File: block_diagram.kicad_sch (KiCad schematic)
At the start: 0 parts

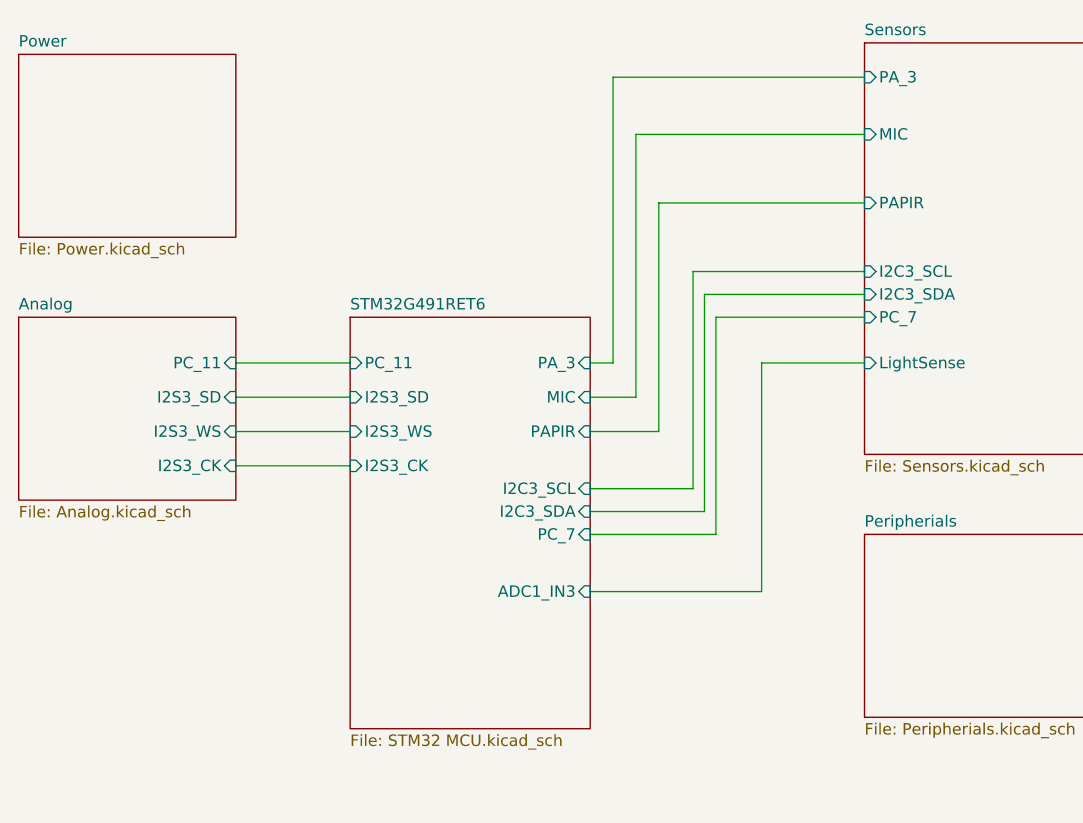
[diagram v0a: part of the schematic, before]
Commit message: fixing audio dac, moving audio to analog section
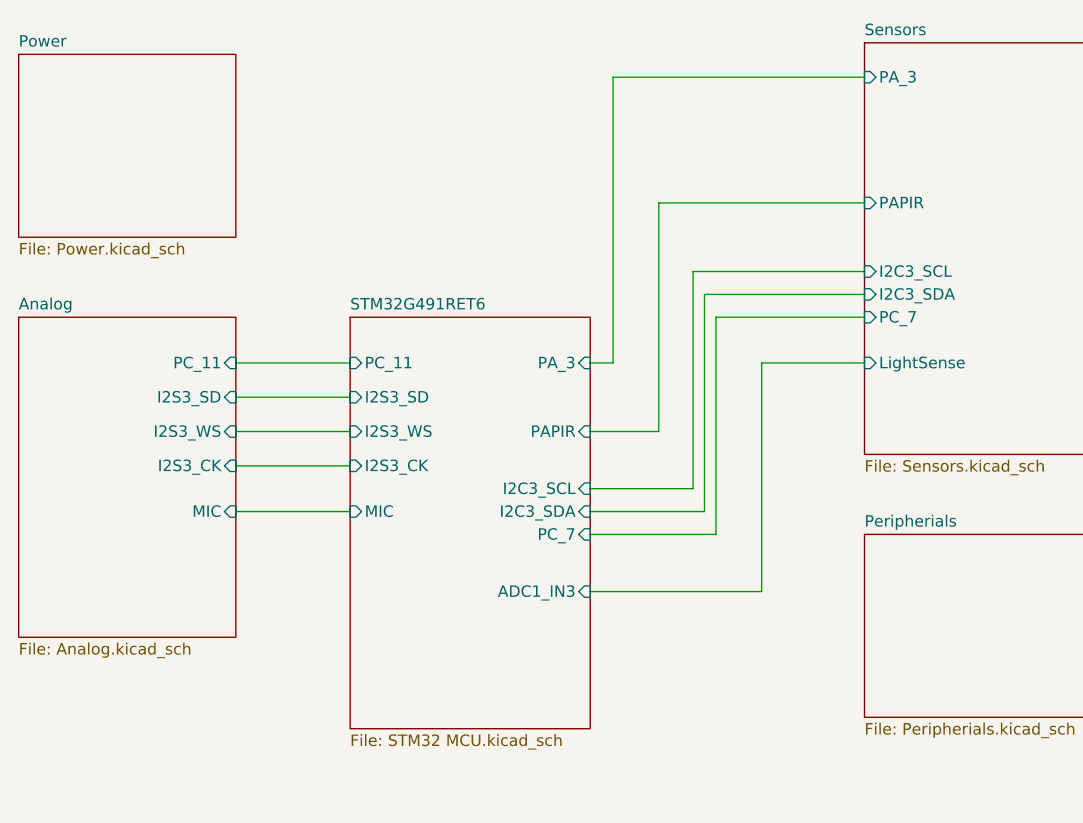
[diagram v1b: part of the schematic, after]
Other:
- sheet Analog ports: added MIC; removed none
- sheet Sensors ports: added none; removed MIC
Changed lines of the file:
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@@
 	(wire
 		(pts
-			(xy 146.05 87.63) (xy 140.97 87.63)
-		)
-		(stroke
-			(width 0)
-			(type default)
-		)
-	)
-	(wire
-		(pts
-			(xy 171.45 58.42) (xy 146.05 58.42)
+			(xy 101.6 100.33) (xy 114.3 100.33)
 		)
 		(stroke
@@
 		)
 	)
-	(wire
-		(pts
-			(xy 146.05 58.42) (xy 146.05 87.63)
-		)
-		(stroke
-			(width 0)
-			(type default)
-		)
-	)
 	(sheet
 		(at 114.3 78.74)
@@
 		)
 		(pin "MIC" input
-			(at 140.97 87.63 0)
-			(effects
-				(font
-					(size 1.27 1.27)
-				)
-				(justify right)
+			(at 114.3 100.33 180)
+			(effects
+				(font
+					(size 1.27 1.27)
+				)
+				(justify left)
 			)
 		)
@@
 			)
 		)
-		(pin "MIC" input
-			(at 171.45 58.42 180)
-			(effects
-				(font
-					(size 1.27 1.27)
-				)
-				(justify left)
-			)
-		)
 		(pin "I2C3_SCL" input
 			(at 171.45 73.66 180)
@@
 	(sheet
 		(at 77.47 78.74)
-		(size 24.13 20.32)
+		(size 24.13 35.56)
 		(exclude_from_sim no)
 		(in_bom yes)
@@
 		)
 		(property "Sheetfile" "Analog.kicad_sch"
-			(at 77.47 99.6446 0)
+			(at 77.47 114.8846 0)
 			(show_name no)
 			(do_not_autoplace no)
@@
 			(effects
 				(font
+					(size 1.27 1.27)
+				)
+				(justify right)
+			)
+		)
+		(pin "MIC" input
+			(at 101.6 100.33 0)
+			(effects
+				(font

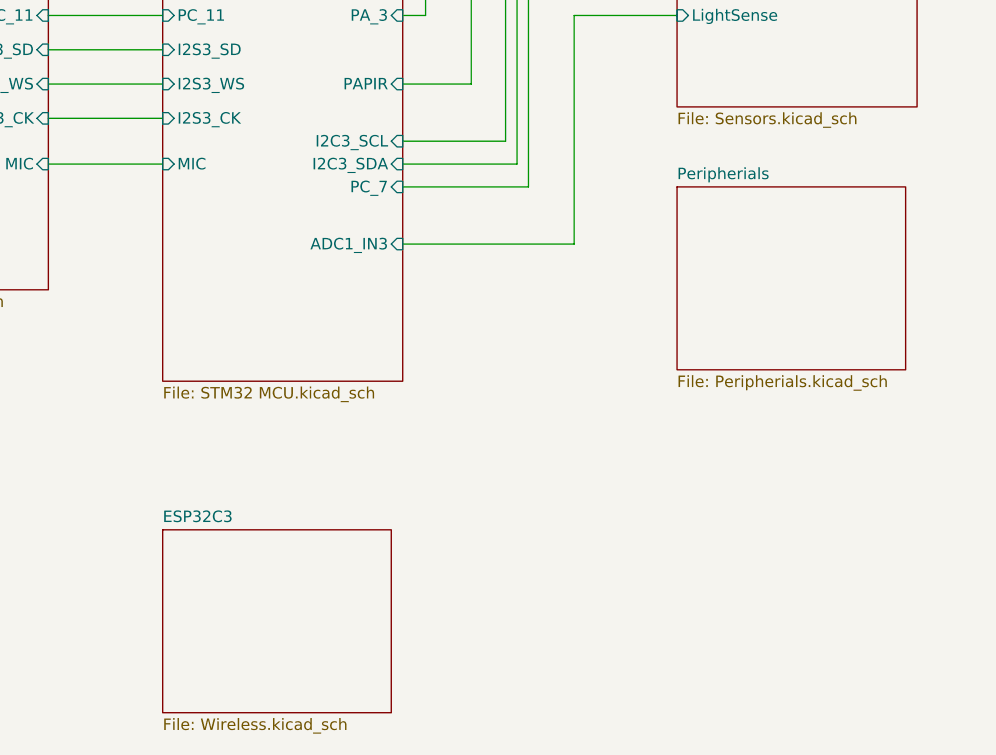
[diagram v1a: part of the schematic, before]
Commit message: added RTC
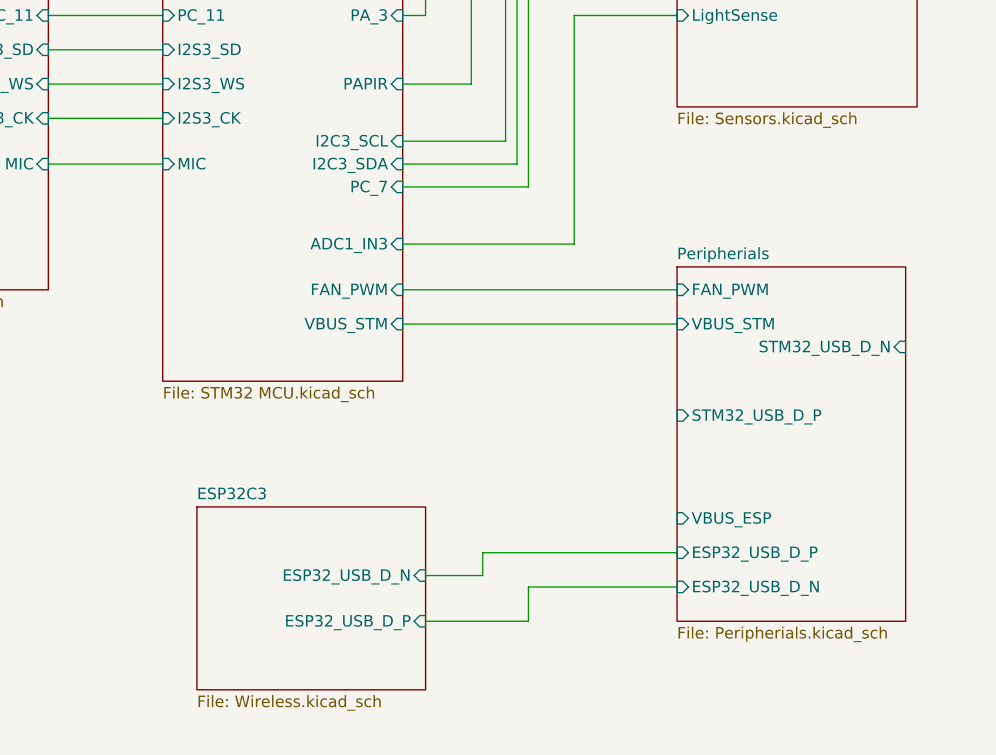
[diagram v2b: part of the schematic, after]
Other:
- sheet ESP32C3 ports: added ESP32_USB_D_N, ESP32_USB_D_P; removed none
- sheet Peripherials ports: added ESP32_USB_D_N, ESP32_USB_D_P, FAN_PWM, STM32_USB_D_N, STM32_USB_D_P, VBUS_ESP, VBUS_STM; removed none
- sheet STM32G491RET6 ports: added FAN_PWM, VBUS_STM; removed none
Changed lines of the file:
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@@
+	(wire
+		(pts
+			(xy 154.94 147.32) (xy 171.45 147.32)
+		)
+		(stroke
+			(width 0)
+			(type default)
+		)
+	)
 	(wire
 		(pts
@@
 	(wire
 		(pts
+			(xy 143.51 151.13) (xy 154.94 151.13)
+		)
+		(stroke
+			(width 0)
+			(type default)
+		)
+	)
+	(wire
+		(pts
+			(xy 140.97 118.11) (xy 171.45 118.11)
+		)
+		(stroke
+			(width 0)
+			(type default)
+		)
+	)
+	(wire
+		(pts
 			(xy 152.4 73.66) (xy 171.45 73.66)
 		)
@@
 	(wire
 		(pts
+			(xy 149.86 143.51) (xy 171.45 143.51)
+		)
+		(stroke
+			(width 0)
+			(type default)
+		)
+	)
+	(wire
+		(pts
 			(xy 101.6 91.44) (xy 114.3 91.44)
 		)
@@
 	(wire
 		(pts
+			(xy 149.86 146.05) (xy 149.86 143.51)
+		)
+		(stroke
+			(width 0)
+			(type default)
+		)
+	)
+	(wire
+		(pts
+			(xy 143.51 146.05) (xy 149.86 146.05)
+		)
+		(stroke
+			(width 0)
+			(type default)
+		)
+	)
+	(wire
+		(pts
 			(xy 140.97 91.44) (xy 148.59 91.44)
 		)
@@
 	(wire
 		(pts
+			(xy 140.97 114.3) (xy 171.45 114.3)
+		)
+		(stroke
+			(width 0)
+			(type default)
+		)
+	)
+	(wire
+		(pts
 			(xy 154.94 78.74) (xy 154.94 102.87)
 		)
@@
 		(pts
 			(xy 101.6 100.33) (xy 114.3 100.33)
+		)
+		(stroke
+			(width 0)
+			(type default)
+		)
+	)
+	(wire
+		(pts
+			(xy 154.94 151.13) (xy 154.94 147.32)
 		)
 		(stroke
@@
 			)
 		)
+		(pin "FAN_PWM" input
+			(at 140.97 114.3 0)
+			(effects
+				(font
+					(size 1.27 1.27)
+				)
+				(justify right)
+			)
+		)
+		(pin "VBUS_STM" input
+			(at 140.97 118.11 0)
+			(effects
+				(font
+					(size 1.27 1.27)
+				)
+				(justify right)
+			)
+		)
 		(instances
 			(project "SeniorDesign_PCB"
@@
 	)
 	(sheet
-		(at 114.3 140.97)
+		(at 118.11 138.43)
 		(size 25.4 20.32)
 		(exclude_from_sim no)
@@
 		)
 		(property "Sheetname" "ESP32C3"
-			(at 114.3 140.2584 0)
+			(at 118.11 137.7184 0)
 			(show_name no)
 			(do_not_autoplace no)
@@
 		)
 		(property "Sheetfile" "Wireless.kicad_sch"
-			(at 114.3 161.8746 0)
+			(at 118.11 159.3346 0)
 			(show_name no)
 			(do_not_autoplace no)
@@
 				)
 				(justify left top)
+			)
+		)
+		(pin "ESP32_USB_D_N" input
+			(at 143.51 146.05 0)
+			(effects
+				(font
+					(size 1.27 1.27)
+				)
+				(justify right)
+			)
+		)
+		(pin "ESP32_USB_D_P" input
+			(at 143.51 151.13 0)
+			(effects
+				(font
+					(size 1.27 1.27)
+				)
+				(justify right)
 			)
 		)
@@
 	)
 	(sheet
-		(at 171.45 102.87)
-		(size 25.4 20.32)
+		(at 171.45 111.76)
+		(size 25.4 39.37)
 		(exclude_from_sim no)
 		(in_bom yes)
@@
 		)
 		(property "Sheetname" "Peripherials"
-			(at 171.45 102.1584 0)
+			(at 171.45 111.0484 0)
 			(show_name no)
 			(do_not_autoplace no)
@@
 		)
 		(property "Sheetfile" "Peripherials.kicad_sch"
-			(at 171.45 123.7746 0)
+			(at 171.45 151.7146 0)
 			(show_name no)
 			(do_not_autoplace no)
@@
 			)
 		)
+		(pin "ESP32_USB_D_N" input
+			(at 171.45 147.32 180)
+			(effects
+				(font
+					(size 1.27 1.27)
+				)
+				(justify left)
+			)
+		)
+		(pin "ESP32_USB_D_P" input
+			(at 171.45 143.51 180)
+			(effects
+				(font
+					(size 1.27 1.27)
+				)
+				(justify left)
+			)
+		)
+		(pin "FAN_PWM" input
+			(at 171.45 114.3 180)
+			(effects
+				(font
+					(size 1.27 1.27)
+				)
+				(justify left)
+			)
+		)
+		(pin "STM32_USB_D_N" input
+			(at 196.85 120.65 0)
+			(effects
+				(font
+					(size 1.27 1.27)
+				)
+				(justify right)
+			)
+		)
+		(pin "STM32_USB_D_P" input
+			(at 171.45 128.27 180)
+			(effects
+				(font
+					(size 1.27 1.27)
+				)
+				(justify left)
+			)
+		)
+		(pin "VBUS_ESP" input
+			(at 171.45 139.7 180)
+			(effects
+				(font
+					(size 1.27 1.27)
+				)
+				(justify left)
+			)
+		)
+		(pin "VBUS_STM" input
+			(at 171.45 118.11 180)
+			(effects
+				(font
+					(size 1.27 1.27)
+				)
+				(justify left)
+			)
+		)

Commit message: hooking stuff up to STM
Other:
- sheet STM32G491RET6 ports: added MIC_ADC; removed MIC

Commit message: block diagram, added flyback on LED
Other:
- sheet Analog ports: added SD_MODE; removed PC_11
- sheet Peripherials ports: added MATRIX_A, MATRIX_B, MATRIX_B1, MATRIX_B2, MATRIX_C, MATRIX_CLK, MATRIX_D, MATRIX_G1, MATRIX_G2, MATRIX_LAT, MATRIX_OE, MATRIX_R1, MATRIX_R2; removed none
- sheet STM32G491RET6 ports: added MATRIX_A, MATRIX_B, MATRIX_B1, MATRIX_B2, MATRIX_C, MATRIX_CLK, MATRIX_D, MATRIX_G1, MATRIX_G2, MATRIX_LAT, MATRIX_OE, MATRIX_R1, MATRIX_R2, SD_MODE; removed PC_11

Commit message: adding duplciate sensors to block diagram
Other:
- added sheet Duplicate Sensors (duplicate_sensors.kicad_sch)
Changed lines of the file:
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@@
+	)
+	(sheet
+		(at 156.21 34.29)
+		(size 22.86 19.05)
+		(exclude_from_sim no)
+		(in_bom yes)
+		(on_board yes)
+		(dnp no)
+		(fields_autoplaced yes)
+		(stroke
+			(width 0.1524)
+			(type solid)
+		)
+		(fill
+			(color 0 0 0 0)
+		)
+		(property "Sheetname" "Duplicate Sensors"
+			(at 156.21 33.5784 0)
+			(show_name no)
+			(do_not_autoplace no)
+			(effects
+				(font
+					(size 1.27 1.27)
+				)
+				(justify left bottom)
+			)
+		)
+		(property "Sheetfile" "duplicate_sensors.kicad_sch"
+			(at 156.21 53.9246 0)
+			(show_name no)
+			(do_not_autoplace no)
+			(effects
+				(font
+					(size 1.27 1.27)
+				)
+				(justify left top)
+			)
+		)
+		(instances
+			(project "SeniorDesign_PCB"
+				(path "/88e1ced0-9576-4565-ab29-f74bf51ccbda"
+					(page "8")
+				)
+			)
+		)
 	)
 	(sheet

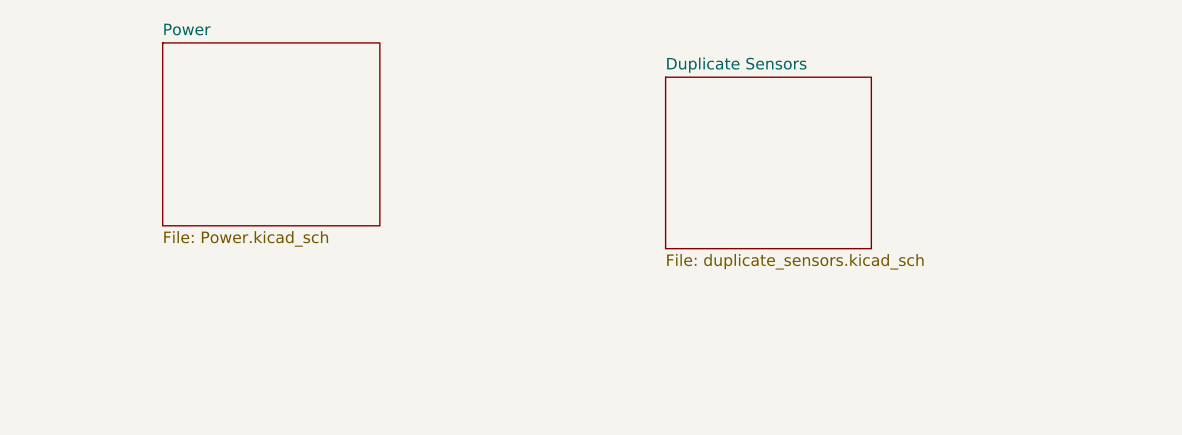
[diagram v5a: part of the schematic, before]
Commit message: footprints on power
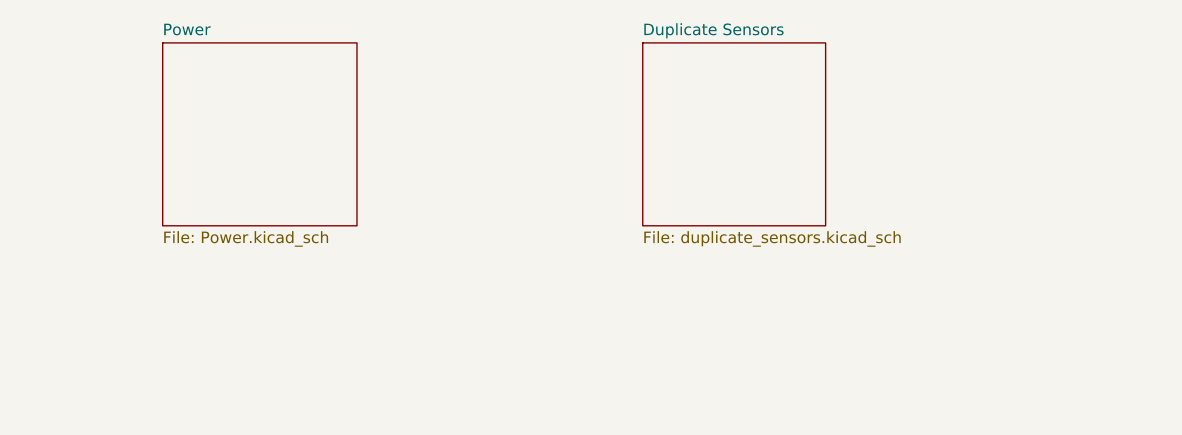
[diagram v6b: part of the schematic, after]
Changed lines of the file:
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@@
 	)
 	(sheet
-		(at 156.21 34.29)
-		(size 22.86 19.05)
+		(at 153.67 30.48)
+		(size 20.32 20.32)
 		(exclude_from_sim no)
 		(in_bom yes)
@@
 		)
 		(property "Sheetname" "Duplicate Sensors"
-			(at 156.21 33.5784 0)
+			(at 153.67 29.7684 0)
 			(show_name no)
 			(do_not_autoplace no)
@@
 		)
 		(property "Sheetfile" "duplicate_sensors.kicad_sch"
-			(at 156.21 53.9246 0)
+			(at 153.67 51.3846 0)
 			(show_name no)
 			(do_not_autoplace no)
@@
 	(sheet
 		(at 100.33 30.48)
-		(size 24.13 20.32)
+		(size 21.59 20.32)
 		(exclude_from_sim no)
 		(in_bom yes)

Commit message: Revert "Merge branch 'main' of https://github.com/pequeno212/PCB_SeniorDesign_team20"
This reverts commit 8ddd870afa6ea88a1f78691f7845b0b29e49b9ae, reversing
changes made to b7b9844e80cb26773f88e7278ccd95378529a98d.
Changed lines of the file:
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@@
 	)
 	(sheet
-		(at 153.67 30.48)
-		(size 20.32 20.32)
+		(at 156.21 34.29)
+		(size 22.86 19.05)
 		(exclude_from_sim no)
 		(in_bom yes)
@@
 		)
 		(property "Sheetname" "Duplicate Sensors"
-			(at 153.67 29.7684 0)
+			(at 156.21 33.5784 0)
 			(show_name no)
 			(do_not_autoplace no)
@@
 		)
 		(property "Sheetfile" "duplicate_sensors.kicad_sch"
-			(at 153.67 51.3846 0)
+			(at 156.21 53.9246 0)
 			(show_name no)
 			(do_not_autoplace no)
@@
 	(sheet
 		(at 100.33 30.48)
-		(size 21.59 20.32)
+		(size 24.13 20.32)
 		(exclude_from_sim no)
 		(in_bom yes)
